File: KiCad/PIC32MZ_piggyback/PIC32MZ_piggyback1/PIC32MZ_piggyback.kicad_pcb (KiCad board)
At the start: 2 copper layers, 53.8 x 53.8 mm, 12 parts, among them J1 Conn_02x13_Odd_Even, J1-1 Conn_01x13_Male, J1-2 Conn_01x13_Male, J2 Conn_02x13_Odd_Even, J2-1 Conn_01x13_Male, J2-2 Conn_01x13_Male, J3 Conn_02x13_Odd_Even, J3-1 Conn_01x13_Male, J3-2 Conn_01x13_Male, J4 Conn_02x13_Odd_Even, J4-1 Conn_01x13_Male, J4-2 Conn_01x13_Male

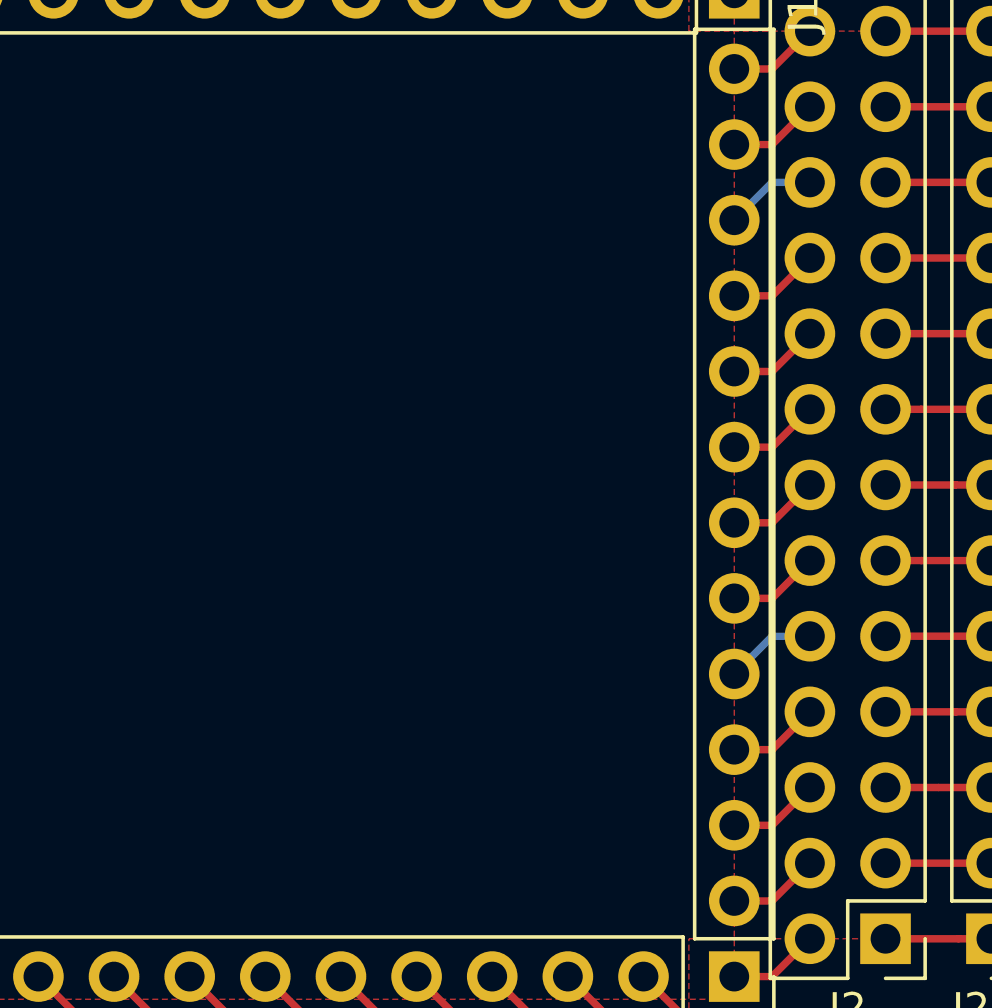
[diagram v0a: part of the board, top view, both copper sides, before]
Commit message: updated new piggyback1 pcb.
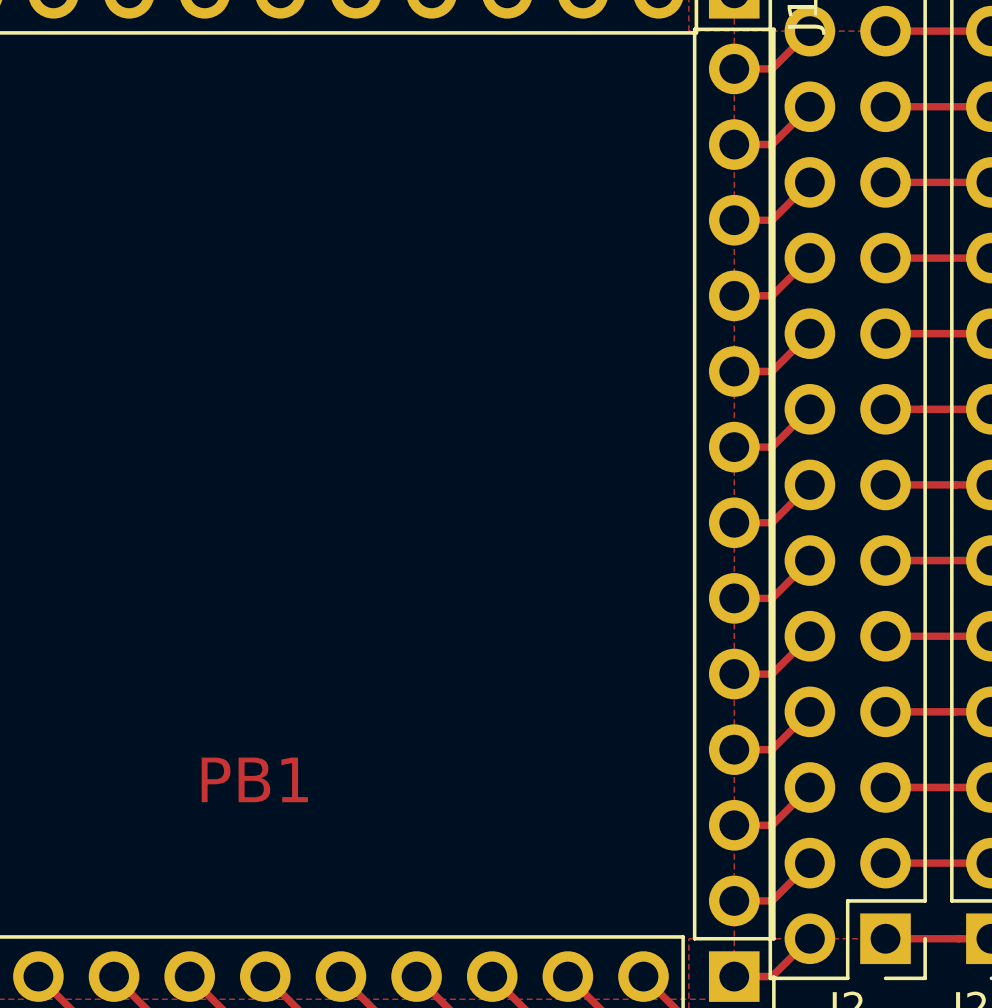
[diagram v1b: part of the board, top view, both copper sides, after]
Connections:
- net Net-(J1-1-Pad10) renamed /RE9
- net Net-(J1-1-Pad11) renamed /RB4
- net Net-(J1-1-Pad12) renamed /RB2
- net Net-(J1-1-Pad13) renamed /RB0
- net Net-(J1-1-Pad2) renamed /TXP
- net Net-(J1-1-Pad3) renamed /RE7
- net Net-(J1-1-Pad5) renamed /RC2
- net Net-(J1-1-Pad7) renamed /RC4
- net Net-(J1-1-Pad8) renamed /RG7
- net Net-(J1-1-Pad9) renamed /RA0
- net Net-(J1-2-Pad1) renamed /TXN
- net Net-(J1-2-Pad10) renamed /RE8
- net Net-(J1-2-Pad11) renamed /RB5
- net Net-(J1-2-Pad12) renamed /RB3
- net Net-(J1-2-Pad13) renamed /RB1
- net Net-(J1-2-Pad4) renamed /RC1
- net Net-(J1-2-Pad6) renamed /RC3
- net Net-(J1-2-Pad7) renamed /RG6
- net Net-(J1-2-Pad8) renamed /RG8
- net Net-(J1-2-Pad9) renamed /RG9
- net Net-(J2-1-Pad1) renamed /RD1
- net Net-(J2-1-Pad10) renamed /RG12
- net Net-(J2-1-Pad11) renamed /RE2
- net Net-(J2-1-Pad12) renamed /RXN
- net Net-(J2-1-Pad2) renamed /RD3
- net Net-(J2-1-Pad3) renamed /RD12
- net Net-(J2-1-Pad4) renamed /RB7
- net Net-(J2-1-Pad6) renamed /RD4
- net Net-(J2-1-Pad7) renamed /RF1
- net Net-(J2-1-Pad9) renamed /RB6
- net Net-(J2-2-Pad1) renamed /RD2
- net Net-(J2-2-Pad10) renamed /RG14
- net Net-(J2-2-Pad12) renamed /RXP
- net Net-(J2-2-Pad13) renamed /RE3
- net Net-(J2-2-Pad2) renamed /RD13
- net Net-(J2-2-Pad4) renamed /RD5
- net Net-(J2-2-Pad7) renamed /RD7
- net Net-(J2-2-Pad8) renamed /RF0
- net Net-(J2-2-Pad9) renamed /RE0
- net Net-(J3-1-Pad10) renamed /RB12
- net Net-(J3-1-Pad11) renamed /RB14
- net Net-(J3-1-Pad12) renamed /RD14
- net Net-(J3-1-Pad13) renamed /RF4
- net Net-(J3-1-Pad4) renamed /RA9
- net Net-(J3-1-Pad5) renamed /RB8
- net Net-(J3-1-Pad6) renamed /RB10
- net Net-(J3-1-Pad7) renamed /MCLR
- net Net-(J3-2-Pad10) renamed /RF12
- net Net-(J3-2-Pad11) renamed /RB13
- net Net-(J3-2-Pad12) renamed /RB15
- net Net-(J3-2-Pad13) renamed /RF5
- net Net-(J3-2-Pad6) renamed /RA10
- net Net-(J3-2-Pad7) renamed /RB9
- net Net-(J3-2-Pad8) renamed /RB11
- net Net-(J3-2-Pad9) renamed /RA1
- net Net-(J4-1-Pad10) renamed /RA4
- net Net-(J4-1-Pad11) renamed /RA14
- net Net-(J4-1-Pad12) renamed /RD10
- net Net-(J4-1-Pad13) renamed /RD0
- net Net-(J4-1-Pad4) renamed /MCU_MISO
- net Net-(J4-1-Pad7) renamed /RA2
- net Net-(J4-2-Pad10) renamed /RA3
- net Net-(J4-2-Pad11) renamed /RA5
- net Net-(J4-2-Pad12) renamed /RA15
- net Net-(J4-2-Pad13) renamed /RD9
- net Net-(J4-2-Pad7) renamed /RF3
- net Net-(J4-2-Pad8) renamed /MCU_SCK
- net Net-(J4-2-Pad9) renamed /MCU_MOSI
- J1 pad 1: Net-(J1-1-Pad1) -> /VCC
- J1 pad 11: Net-(J1-1-Pad6) -> /VCC
- J1 pad 6: Net-(J1-2-Pad3) -> /VCC
- J1-1 pad 1: Net-(J1-1-Pad1) -> /VCC
- J1-1 pad 6: Net-(J1-1-Pad6) -> /VCC
- J1-2 pad 3: Net-(J1-2-Pad3) -> /VCC
- J2 pad 12: Net-(J2-2-Pad6) -> /VCC
- J2 pad 25: Net-(J2-1-Pad13) -> /VCC
- J2 pad 9: Net-(J2-1-Pad5) -> /VCC
- J2-1 pad 13: Net-(J2-1-Pad13) -> /VCC
- J2-1 pad 5: Net-(J2-1-Pad5) -> /VCC
- J2-2 pad 6: Net-(J2-2-Pad6) -> /VCC
- J3 pad 17: Net-(J3-1-Pad9) -> /VCC
- J3 pad 3: Net-(J3-1-Pad2) -> /LED1
- J3 pad 5: Net-(J3-1-Pad3) -> /LED2
- J3-1 pad 2: Net-(J3-1-Pad2) -> /LED1
- J3-1 pad 3: Net-(J3-1-Pad3) -> /LED2
- J3-1 pad 9: Net-(J3-1-Pad9) -> /VCC
- J4 pad 10: Net-(J4-2-Pad5) -> /LED2
- J4 pad 12: Net-(J4-2-Pad6) -> /VCC
- J4 pad 4: Net-(J4-2-Pad2) -> /VCC
- J4 pad 5: Net-(J4-1-Pad3) -> /VCC
- J4 pad 9: Net-(J4-1-Pad5) -> /LED1
- J4-1 pad 3: Net-(J4-1-Pad3) -> /VCC
- J4-1 pad 5: Net-(J4-1-Pad5) -> /LED1
- J4-2 pad 2: Net-(J4-2-Pad2) -> /VCC
- J4-2 pad 5: Net-(J4-2-Pad5) -> /LED2
- J4-2 pad 6: Net-(J4-2-Pad6) -> /VCC
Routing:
- net /VCC: track 0.00 -> 34.7 mm
- net /LED1: track 0.00 -> 7.11 mm
- net /LED2: track 0.00 -> 6.98 mm
- net Net-(J2-1-Pad5): track 3.56 -> 0.00 mm
- net Net-(J2-1-Pad13): track 3.56 -> 0.00 mm
- net Net-(J4-1-Pad5): track 3.56 -> 0.00 mm
- net Net-(J4-1-Pad3): track 3.56 -> 0.00 mm
- net Net-(J3-1-Pad9): track 3.56 -> 0.00 mm
- net Net-(J3-1-Pad3): track 3.56 -> 0.00 mm
- net Net-(J3-1-Pad2): track 3.56 -> 0.00 mm
- net Net-(J1-1-Pad6): track 3.56 -> 0.00 mm
- net Net-(J1-1-Pad1): track 3.56 -> 0.00 mm
- net Net-(J1-2-Pad3): track 3.43 -> 0.00 mm
- net Net-(J4-2-Pad6): track 3.43 -> 0.00 mm
- net Net-(J4-2-Pad5): track 3.43 -> 0.00 mm
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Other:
- board text added: "PB1"
